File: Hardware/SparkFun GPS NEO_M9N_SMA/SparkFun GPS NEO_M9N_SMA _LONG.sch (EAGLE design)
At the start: 52 parts, among them J2 Qwiic Right Angle, J4 Qwiic Right Angle, U1 U-BLOX_NEO-M9N, U2 3.3V

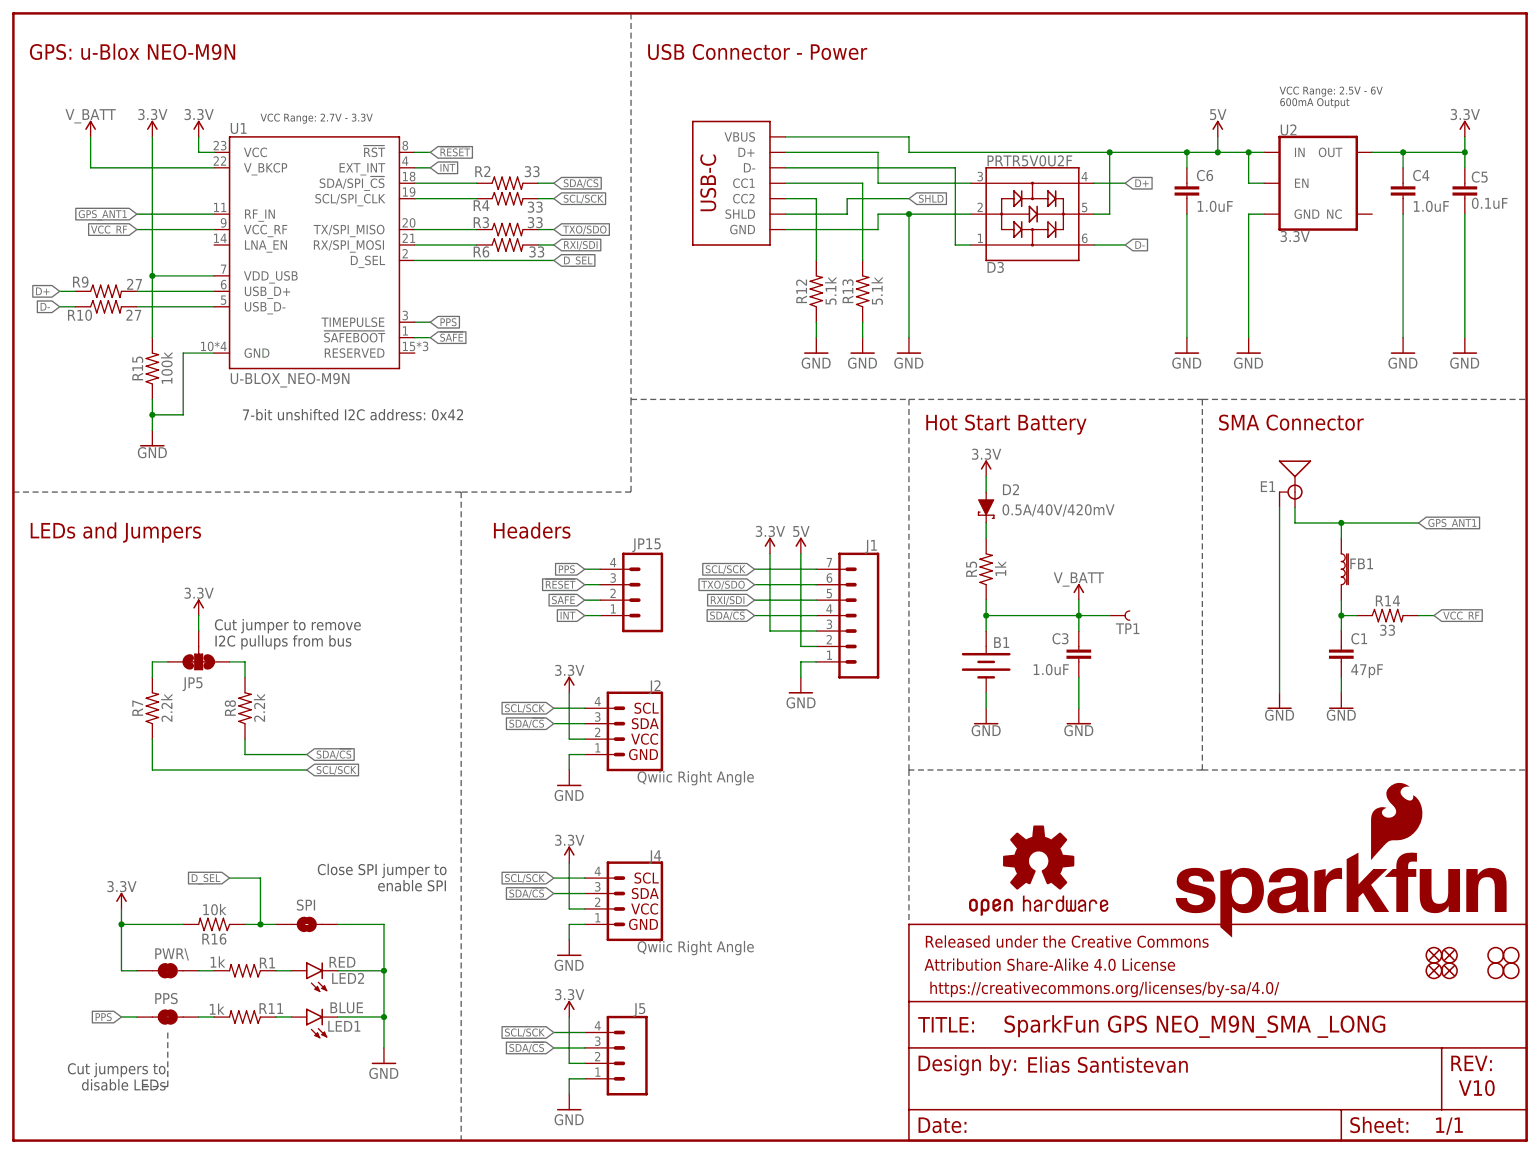
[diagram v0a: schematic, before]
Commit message: Adds some text for L1/L2 band support on the schematic
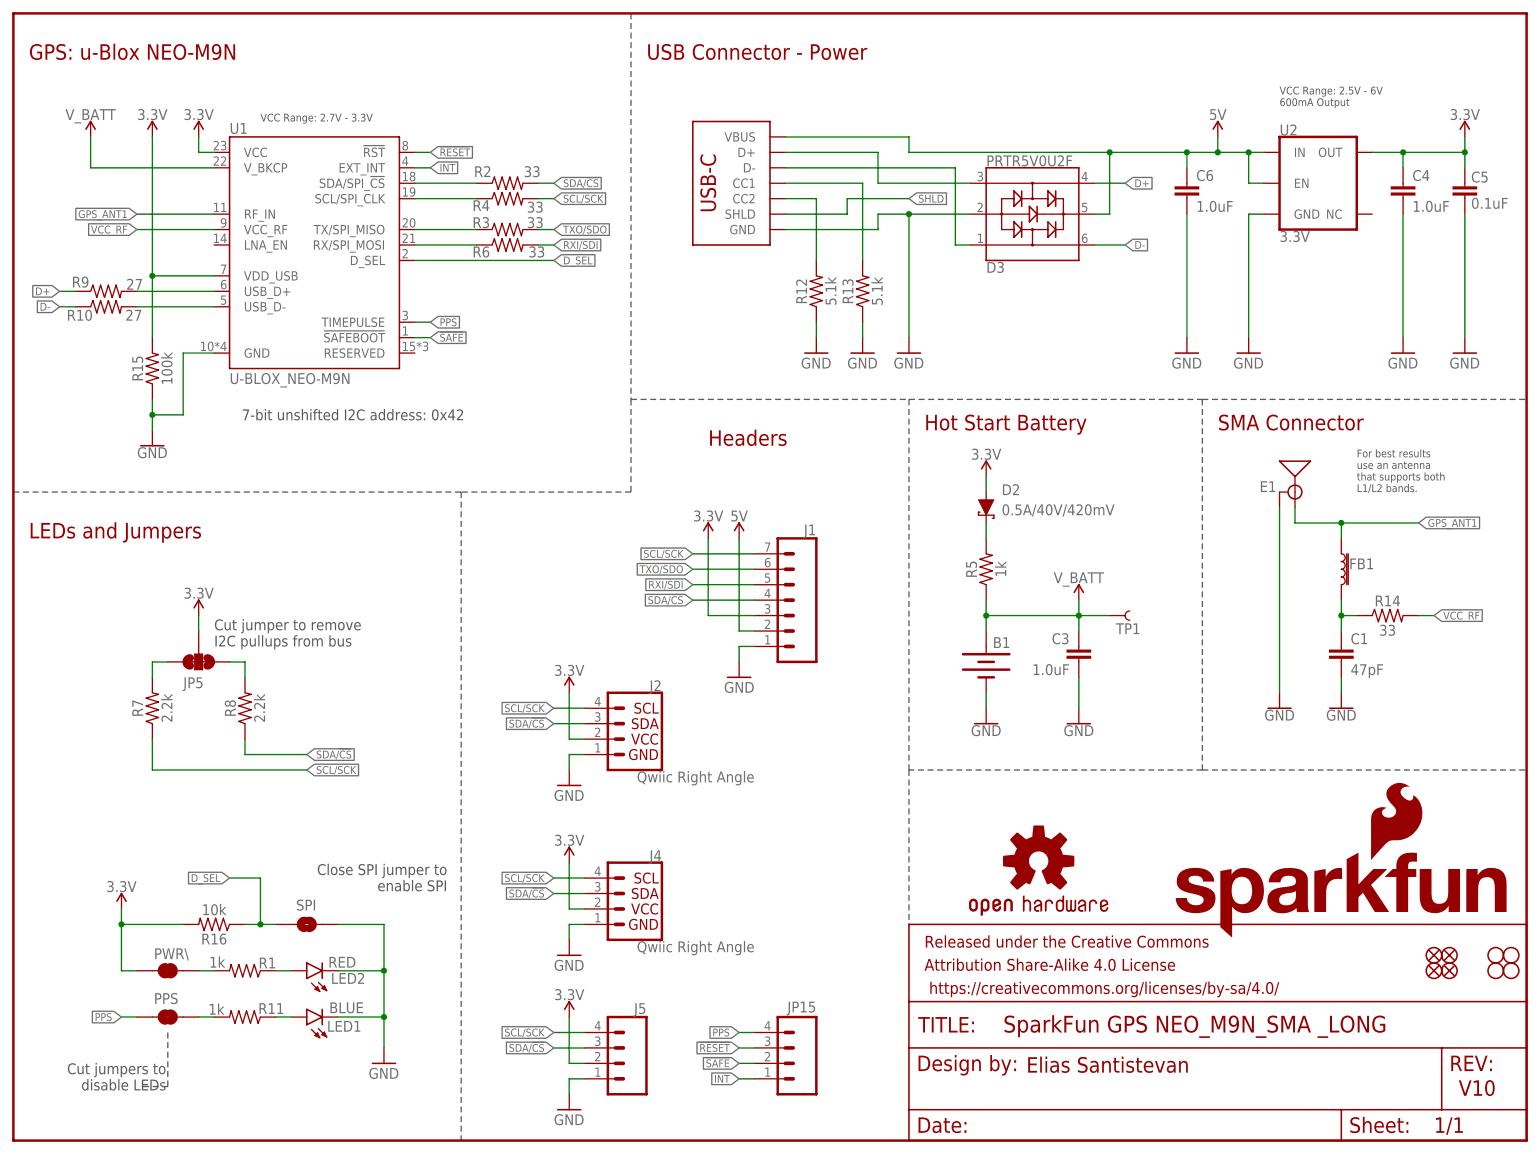
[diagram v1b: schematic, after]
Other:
- note added: "For best results use an antenna that supports both L1/L2 bands."
- moved on the sheet: J1, JP15
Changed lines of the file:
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@@
 enable SPI</text>
 <text x="166.624" y="11.176" size="2.54" layer="94" font="vector">Elias Santistevan</text>
-<text x="78.74" y="99.06" size="2.54" layer="94" font="vector">Headers</text>
+<text x="114.3" y="114.3" size="2.54" layer="94" font="vector">Headers</text>
 <text x="2.54" y="99.06" size="2.54" layer="94" font="vector">LEDs and Jumpers</text>
 <text x="149.86" y="116.84" size="2.54" layer="94" font="vector">Hot Start Battery</text>
@@
 <text x="208.28" y="170.18" size="1.27" layer="97" font="vector">VCC Range: 2.5V - 6V
 600mA Output</text>
+<text x="220.98" y="106.68" size="1.27" layer="97" font="vector">For best results
+use an antenna
+that supports both
+L1/L2 bands.</text>
 </plain>
 <instances>
@@
 <instance part="JP91" gate="G$1" x="243.84" y="30.48" smashed="yes"/>
 <instance part="JP101" gate="G$1" x="243.84" y="27.94" smashed="yes"/>
-<instance part="GND1" gate="1" x="129.54" y="73.66" smashed="yes" rot="MR0">
-<attribute name="VALUE" x="132.08" y="71.12" size="1.778" layer="96" font="vector" rot="MR0"/>
+<instance part="GND1" gate="1" x="119.38" y="76.2" smashed="yes" rot="MR0">
+<attribute name="VALUE" x="121.92" y="73.66" size="1.778" layer="96" font="vector" rot="MR0"/>
 </instance>
 <instance part="GND15" gate="1" x="132.08" y="129.54" smashed="yes">
@@
 <attribute name="VALUE" x="22.86" y="167.894" size="1.778" layer="96" font="vector" rot="MR0" align="bottom-center"/>
 </instance>
-<instance part="JP15" gate="J1" x="101.6" y="88.9" smashed="yes" rot="MR0">
-<attribute name="VALUE" x="106.68" y="78.74" size="1.778" layer="96" rot="MR0"/>
-<attribute name="NAME" x="106.68" y="97.282" size="1.778" layer="95" font="vector" rot="MR0"/>
-</instance>
-<instance part="SUPPLY10" gate="G$1" x="124.46" y="96.52" smashed="yes">
-<attribute name="VALUE" x="124.46" y="99.314" size="1.778" layer="96" font="vector" align="bottom-center"/>
-</instance>
-<instance part="J1" gate="J1" x="137.16" y="83.82" smashed="yes" rot="MR0">
-<attribute name="VALUE" x="142.24" y="73.914" size="1.778" layer="96" font="vector" rot="MR0"/>
-<attribute name="NAME" x="142.24" y="97.028" size="1.778" layer="95" font="vector" rot="MR0"/>
-</instance>
-<instance part="SUPPLY11" gate="G$1" x="129.54" y="96.52" smashed="yes">
-<attribute name="VALUE" x="129.54" y="99.314" size="1.778" layer="96" font="vector" align="bottom-center"/>
+<instance part="JP15" gate="J1" x="127" y="12.7" smashed="yes" rot="MR0">
+<attribute name="VALUE" x="132.08" y="2.54" size="1.778" layer="96" rot="MR0"/>
+<attribute name="NAME" x="132.08" y="21.082" size="1.778" layer="95" font="vector" rot="MR0"/>
+</instance>
+<instance part="SUPPLY10" gate="G$1" x="114.3" y="99.06" smashed="yes">
+<attribute name="VALUE" x="114.3" y="101.854" size="1.778" layer="96" font="vector" align="bottom-center"/>
+</instance>
+<instance part="J1" gate="J1" x="127" y="86.36" smashed="yes" rot="MR0">
+<attribute name="VALUE" x="132.08" y="76.454" size="1.778" layer="96" font="vector" rot="MR0"/>
+<attribute name="NAME" x="132.08" y="99.568" size="1.778" layer="95" font="vector" rot="MR0"/>
+</instance>
+<instance part="SUPPLY11" gate="G$1" x="119.38" y="99.06" smashed="yes">
+<attribute name="VALUE" x="119.38" y="101.854" size="1.778" layer="96" font="vector" align="bottom-center"/>
 </instance>
 <instance part="LOGO2" gate="G$1" x="190.5" y="33.02" smashed="yes"/>
@@
 </segment>
 <segment>
-<wire x1="124.46" y1="83.82" x2="124.46" y2="96.52" width="0.1524" layer="91"/>
-<wire x1="132.08" y1="83.82" x2="124.46" y2="83.82" width="0.1524" layer="91"/>
+<wire x1="114.3" y1="86.36" x2="114.3" y2="99.06" width="0.1524" layer="91"/>
+<wire x1="121.92" y1="86.36" x2="114.3" y2="86.36" width="0.1524" layer="91"/>
 <pinref part="SUPPLY10" gate="G$1" pin="3.3V"/>
 <pinref part="J1" gate="J1" pin="3"/>
@@
 <pinref part="J1" gate="J1" pin="1"/>
 <pinref part="GND1" gate="1" pin="GND"/>
-<wire x1="132.08" y1="78.74" x2="129.54" y2="78.74" width="0.1524" layer="91"/>
-<wire x1="129.54" y1="78.74" x2="129.54" y2="76.2" width="0.1524" layer="91"/>
+<wire x1="121.92" y1="81.28" x2="119.38" y2="81.28" width="0.1524" layer="91"/>
+<wire x1="119.38" y1="81.28" x2="119.38" y2="78.74" width="0.1524" layer="91"/>
 </segment>
 <segment>
@@
 </segment>
 <segment>
-<wire x1="132.08" y1="93.98" x2="121.92" y2="93.98" width="0.1524" layer="91"/>
-<label x="121.92" y="93.98" size="1.27" layer="95" font="vector" rot="MR0" xref="yes"/>
+<wire x1="121.92" y1="96.52" x2="111.76" y2="96.52" width="0.1524" layer="91"/>
+<label x="111.76" y="96.52" size="1.27" layer="95" font="vector" rot="MR0" xref="yes"/>
 <pinref part="J1" gate="J1" pin="7"/>
 </segment>
@@
 </segment>
 <segment>
-<wire x1="132.08" y1="86.36" x2="121.92" y2="86.36" width="0.1524" layer="91"/>
-<label x="121.92" y="86.36" size="1.27" layer="95" font="vector" rot="MR0" xref="yes"/>
+<wire x1="121.92" y1="88.9" x2="111.76" y2="88.9" width="0.1524" layer="91"/>
+<label x="111.76" y="88.9" size="1.27" layer="95" font="vector" rot="MR0" xref="yes"/>
 <pinref part="J1" gate="J1" pin="4"/>
 </segment>
@@
 </segment>
 <segment>
-<wire x1="96.52" y1="91.44" x2="93.98" y2="91.44" width="0.1524" layer="91"/>
-<label x="93.98" y="91.44" size="1.27" layer="95" font="vector" rot="MR0" xref="yes"/>
+<wire x1="121.92" y1="15.24" x2="119.38" y2="15.24" width="0.1524" layer="91"/>
+<label x="119.38" y="15.24" size="1.27" layer="95" font="vector" rot="MR0" xref="yes"/>
 <pinref part="JP15" gate="J1" pin="3"/>
 </segment>
@@
 </segment>
 <segment>
-<wire x1="96.52" y1="86.36" x2="93.98" y2="86.36" width="0.1524" layer="91"/>
-<label x="93.98" y="86.36" size="1.27" layer="95" font="vector" rot="MR0" xref="yes"/>
+<wire x1="121.92" y1="10.16" x2="119.38" y2="10.16" width="0.1524" layer="91"/>
+<label x="119.38" y="10.16" size="1.27" layer="95" font="vector" rot="MR0" xref="yes"/>
 <pinref part="JP15" gate="J1" pin="1"/>
 </segment>
@@
 </segment>
 <segment>
-<wire x1="96.52" y1="93.98" x2="93.98" y2="93.98" width="0.1524" layer="91"/>
-<label x="93.98" y="93.98" size="1.27" layer="95" font="vector" rot="MR0" xref="yes"/>
+<wire x1="121.92" y1="17.78" x2="119.38" y2="17.78" width="0.1524" layer="91"/>
+<label x="119.38" y="17.78" size="1.27" layer="95" font="vector" rot="MR0" xref="yes"/>
 <pinref part="JP15" gate="J1" pin="4"/>
 </segment>
@@
 </segment>
 <segment>
-<wire x1="96.52" y1="88.9" x2="93.98" y2="88.9" width="0.1524" layer="91"/>
-<label x="93.98" y="88.9" size="1.27" layer="95" font="vector" rot="MR0" xref="yes"/>
+<wire x1="121.92" y1="12.7" x2="119.38" y2="12.7" width="0.1524" layer="91"/>
+<label x="119.38" y="12.7" size="1.27" layer="95" font="vector" rot="MR0" xref="yes"/>
 <pinref part="JP15" gate="J1" pin="2"/>
 </segment>
@@
 </segment>
 <segment>
-<wire x1="132.08" y1="88.9" x2="121.92" y2="88.9" width="0.1524" layer="91"/>
-<label x="121.92" y="88.9" size="1.27" layer="95" font="vector" rot="MR0" xref="yes"/>
+<wire x1="121.92" y1="91.44" x2="111.76" y2="91.44" width="0.1524" layer="91"/>
+<label x="111.76" y="91.44" size="1.27" layer="95" font="vector" rot="MR0" xref="yes"/>
 <pinref part="J1" gate="J1" pin="5"/>
 </segment>
@@
 </segment>
 <segment>
-<wire x1="132.08" y1="91.44" x2="121.92" y2="91.44" width="0.1524" layer="91"/>
-<label x="121.92" y="91.44" size="1.27" layer="95" font="vector" rot="MR0" xref="yes"/>
+<wire x1="121.92" y1="93.98" x2="111.76" y2="93.98" width="0.1524" layer="91"/>
+<label x="111.76" y="93.98" size="1.27" layer="95" font="vector" rot="MR0" xref="yes"/>
 <pinref part="J1" gate="J1" pin="6"/>
 </segment>
@@
 <segment>
 <pinref part="J1" gate="J1" pin="2"/>
-<wire x1="132.08" y1="81.28" x2="129.54" y2="81.28" width="0.1524" layer="91"/>
-<wire x1="129.54" y1="81.28" x2="129.54" y2="96.52" width="0.1524" layer="91"/>
+<wire x1="121.92" y1="83.82" x2="119.38" y2="83.82" width="0.1524" layer="91"/>
+<wire x1="119.38" y1="83.82" x2="119.38" y2="99.06" width="0.1524" layer="91"/>
 <pinref part="SUPPLY11" gate="G$1" pin="5V"/>
 </segment>
